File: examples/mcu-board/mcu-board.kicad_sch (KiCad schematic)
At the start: 11 parts, among them J1 5V_IN, J2 PROG/IO, SW1 Reset, U1 MCU, U2 AMS1117-3.3

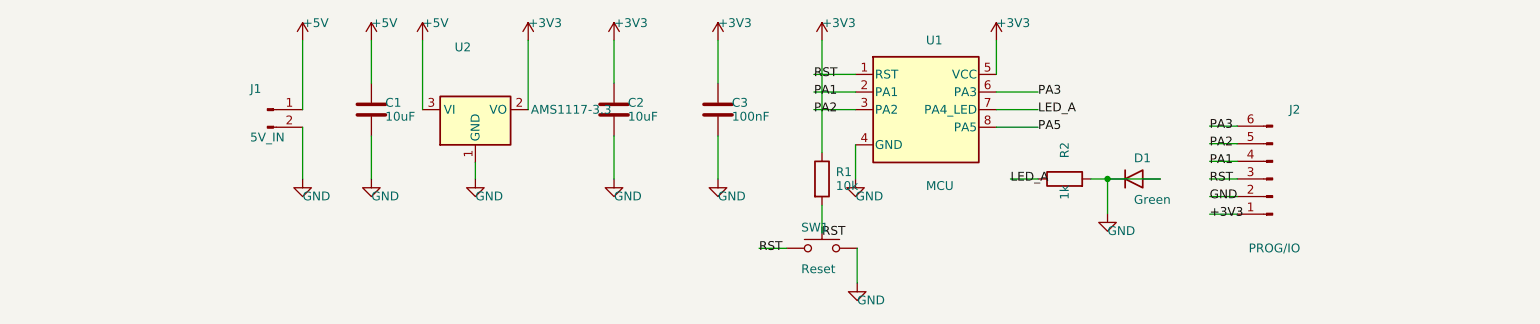
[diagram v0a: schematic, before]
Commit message: examples/mcu-board: swap to system-library footprints
Replaces every inline footprint with a proper KiCad system-library
match — body silk, fab outline, courtyard, and pin-1 indicator now
travel with the part instead of being faked as separate board-level
shapes.

Workflow:
  - lib_assign_footprint to set the schematic Footprint property on
    each symbol (Package_SO:SOIC-8_3.9x4.9mm_P1.27mm,
    Package_TO_SOT_SMD:SOT-223-3_TabPin2,
    Capacitor_SMD:C_0805_2012Metric, etc.)
  - pcb_sync_from_schematic with replace_mismatched=True force=True to
    pull the new footprint definitions into the existing pads
  - delete the five board-level F.SilkS rectangles I had added as
    stand-in body outlines; the IPC-7351 footprints carry their own

Net coverage stays clean (100% pad coverage in the sync report).
ERC violations from the placeholder MCU symbol persist; they're
override-only for now and will get resolved when the schematic
symbols themselves are tightened.

Co-Authored-By: Claude Opus 4.7 (1M context) <noreply@anthropic.com>
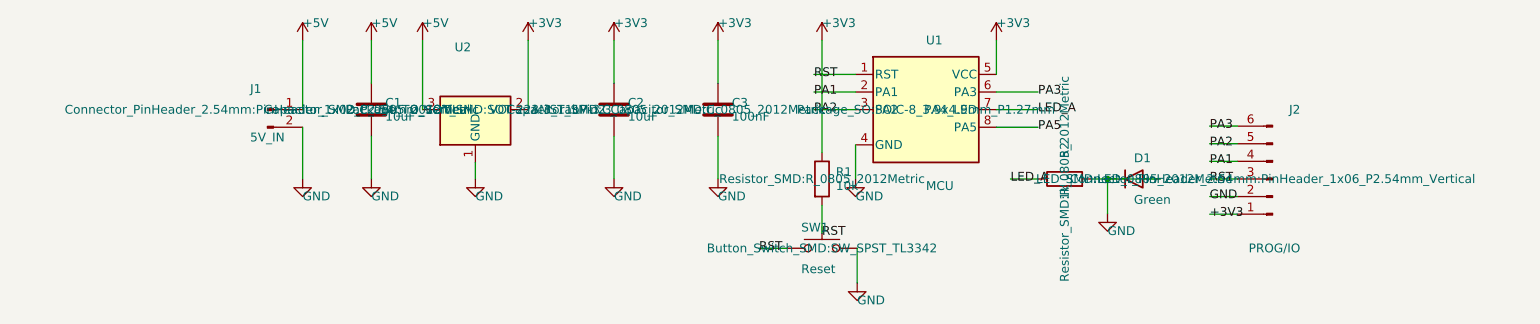
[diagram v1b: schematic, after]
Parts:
- C1, C2, C3: footprint (none) -> Capacitor_SMD:C_0805_2012Metric
- D1: footprint (none) -> LED_SMD:LED_0805_2012Metric
- J1: footprint (none) -> Connector_PinHeader_2.54mm:PinHeader_1x02_P2.54mm_Vertical
- J2: footprint (none) -> Connector_PinHeader_2.54mm:PinHeader_1x06_P2.54mm_Vertical
- R1, R2: footprint (none) -> Resistor_SMD:R_0805_2012Metric
- SW1: footprint (none) -> Button_Switch_SMD:SW_SPST_TL3342
- U1: footprint (none) -> Package_SO:SOIC-8_3.9x4.9mm_P1.27mm
- U2: footprint (none) -> Package_TO_SOT_SMD:SOT-223-3_TabPin2

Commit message: examples/mcu-board: fix R2-D1 anode short, drop stale silk, hide footprint labels
Three follow-ups on the previous routing pass:

- Reroute the schematic wire from R2.2 to D1.A around D1.1 (cathode).
  The straight horizontal wire at y=95 from (168.81, 95) to (178.81,
  95) was passing right through D1's cathode pad at (171.19, 95),
  shorting the LED-anode net to GND through the cathode. Replaced
  with a 3-segment detour at y=92.
- Delete the leftover F.SilkS rectangle at (145.5, 114.5)..(150.5,
  119.5). It was a hand-placed body outline for SW1 from before SW1
  was rotated and moved to (150, 138); after the move it became an
  empty box hovering above the LED chain.
- Hide the Footprint property text on every schematic symbol
  instance. KiCad's pcb_sync_from_schematic round-trip had set them
  visible, leaving the schematic cluttered with strings like
  "Resistor_SMD:R_0805_2012Metric" overlapping the value labels.
  Re-flipped to (hide yes) on all 38 Footprint property blocks.

Co-Authored-By: Claude Opus 4.7 (1M context) <noreply@anthropic.com>
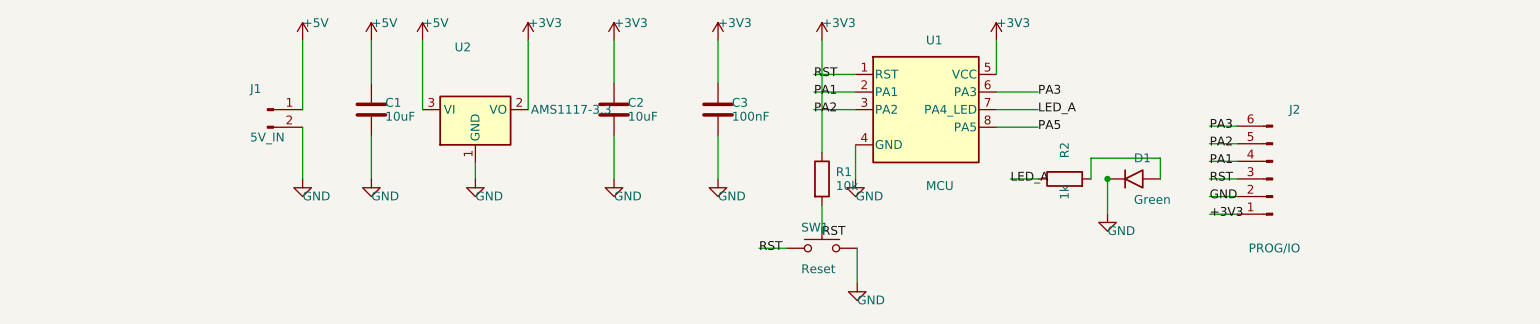
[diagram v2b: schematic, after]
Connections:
- net GND: no longer D1.2 (A), R2.2
- new net: D1.2 (A), R2.2
